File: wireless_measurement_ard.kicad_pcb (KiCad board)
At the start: 2 copper layers, 70 x 21.2 mm, 22 parts, among them J1 Conn_01x08, SW1 SW_SPDT, U2 JDY-08, U3 MCP16415, U4 MAX9938, U5 MAX9938, U6 EFM8LB1x-QFP32

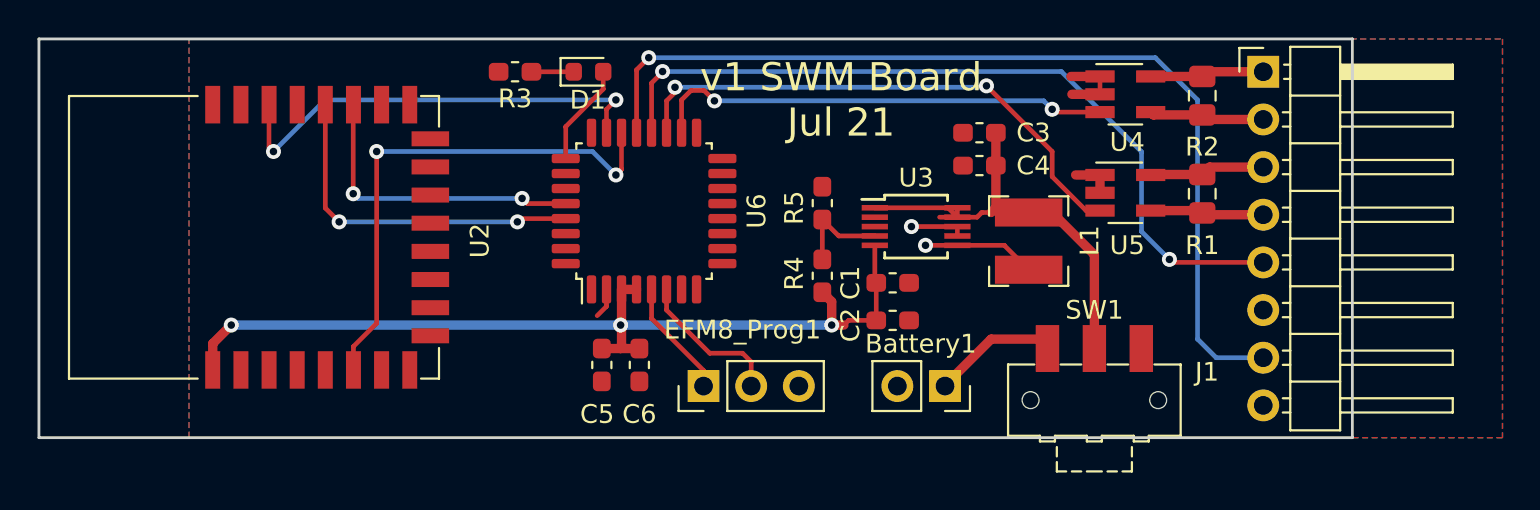
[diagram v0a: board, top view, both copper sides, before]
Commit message: update kicad to include holes
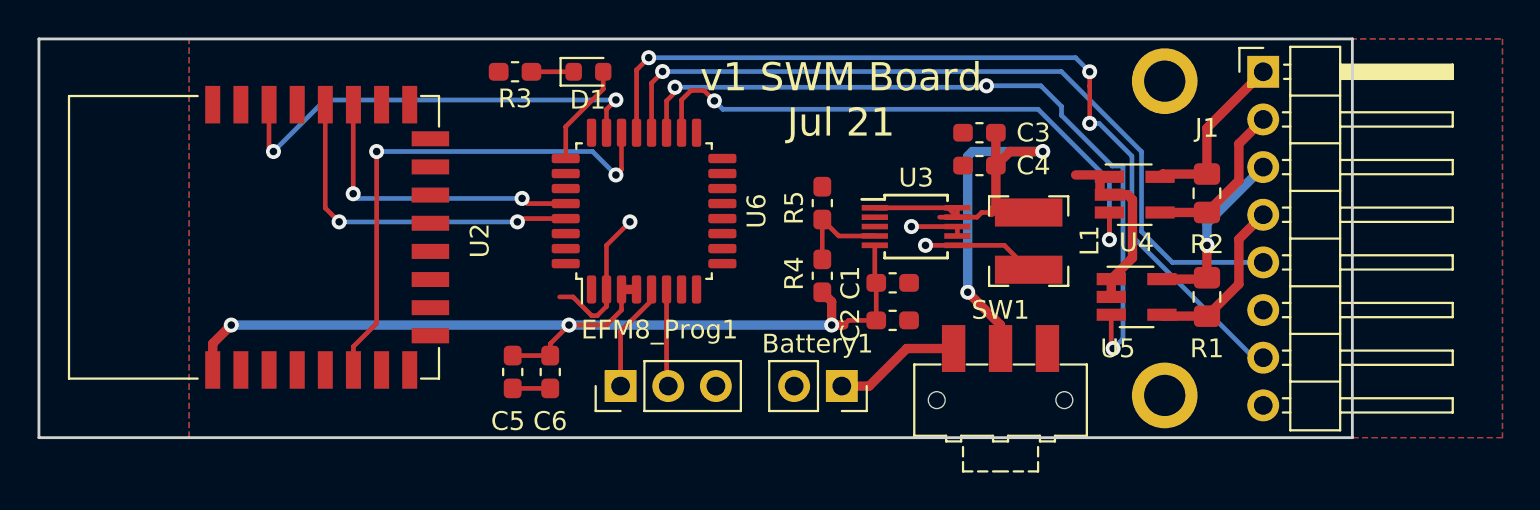
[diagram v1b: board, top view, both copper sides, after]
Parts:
- added H1: MountingHole_Pad, MountingHole:MountingHole_2.2mm_M2_ISO7380_Pad, F.Cu at (170.0, 94.0)
- added H2: MountingHole_Pad, MountingHole:MountingHole_2.2mm_M2_ISO7380_Pad, F.Cu at (170.0, 77.2)
- moved U5 5.58 mm to (168.5, 88.8)
- moved R1 5.51 mm to (172.2, 88.8)
- moved Battery1 5.50 mm to (152.8, 93.5)
- moved U4 5.37 mm to (168.4, 83.3)
- moved R2 5.21 mm to (172.2, 83.2)
- moved SW1 5.00 mm to (161.2, 94.2)
- moved C5 4.76 mm to (135.2, 92.8)
- moved C6 4.76 mm to (137.2, 92.8)
- moved EFM8_Prog1 4.42 mm to (141.0, 93.5)
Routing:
- net GND: track 10.8 -> 22.3 mm, vias 1 -> 2
- net A1: track 28.9 -> 40.4 mm, vias 2 -> 3
- net VIN: track 24.2 -> 33.5 mm, vias 0 -> 2
- net A0: track 24.7 -> 31.3 mm
- net C2_IN: track 6.17 -> 9.57 mm, vias 0 -> 1
- net A3: track 51.1 -> 47.7 mm, vias 1 -> 3
- net C1_IN: track 6.10 -> 9.25 mm
- net C2_OUT: track 6.09 -> 9.08 mm
- net +3V3: track 49.5 -> 52.3 mm
- net C2D: track 8.04 -> 5.19 mm
- net C1_OUT: track 6.16 -> 8.70 mm
- net Net-(SW1-Pad3): track 0.00 -> 0.85 mm
- net BATT: track 7.33 -> 6.79 mm
- net A2: vias 2 -> 1

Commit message: update to fix VIO
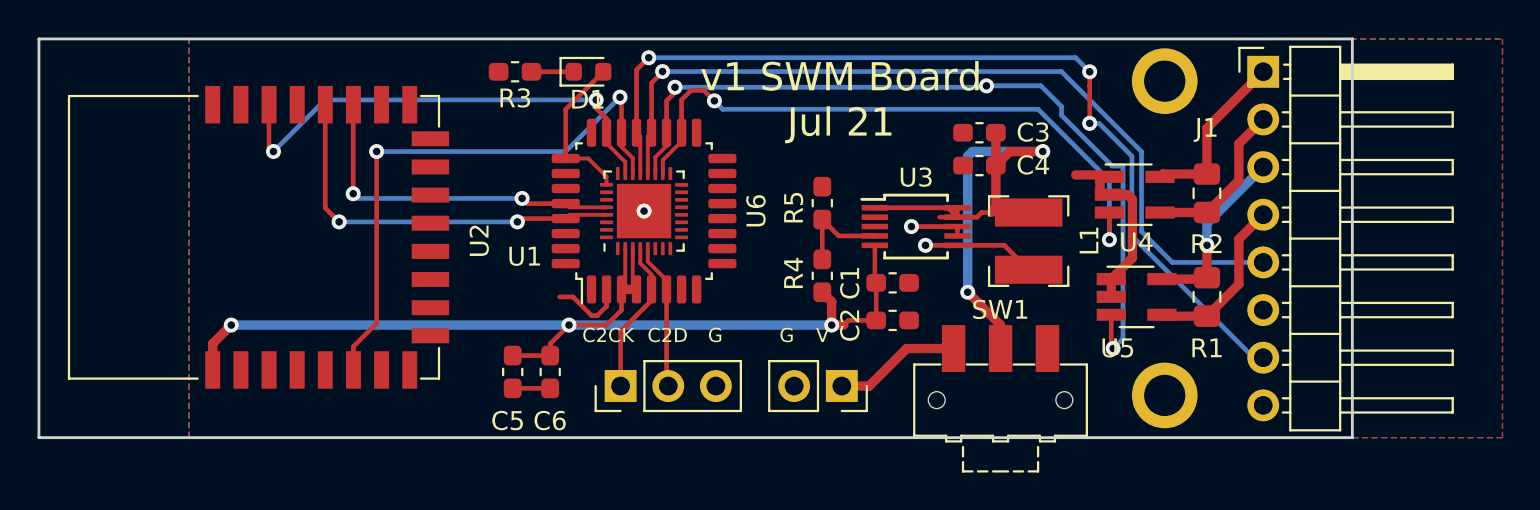
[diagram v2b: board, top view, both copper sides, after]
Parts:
- added U1: EFM8LB1, Package_DFN_QFN:QFN-32-1EP_4x4mm_P0.4mm_EP2.9x2.9mm, F.Cu at (142.2, 84.2)
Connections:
- net Net-(D1-Pad2) renamed LED
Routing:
- net +3V3: track 52.3 -> 56.9 mm
- net GND: track 22.3 -> 18.2 mm
- net LED: track 5.45 -> 8.46 mm
- net STATUS: track 27.8 -> 30.7 mm
- net C2D: track 5.19 -> 7.78 mm
- net A0: track 31.3 -> 33.9 mm
- net C2CK: track 5.83 -> 8.26 mm
- net A1: track 40.4 -> 42.9 mm
- net ARD_TX: track 18.7 -> 21.0 mm
- net A3: track 47.7 -> 50.0 mm
- net A2: track 42.2 -> 44.5 mm
- net ARD_RX: track 16.3 -> 18.6 mm
- net PWRC: track 23.9 -> 25.5 mm
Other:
- net class Default: clearance 0.2 -> 0.13
- rule trace_clearance: 0.2 -> 0.13
- board text added: "C2CK"
- board text added: "C2D"
- board text added: "G"
- board text added: "V"

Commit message: Halved the size of the board
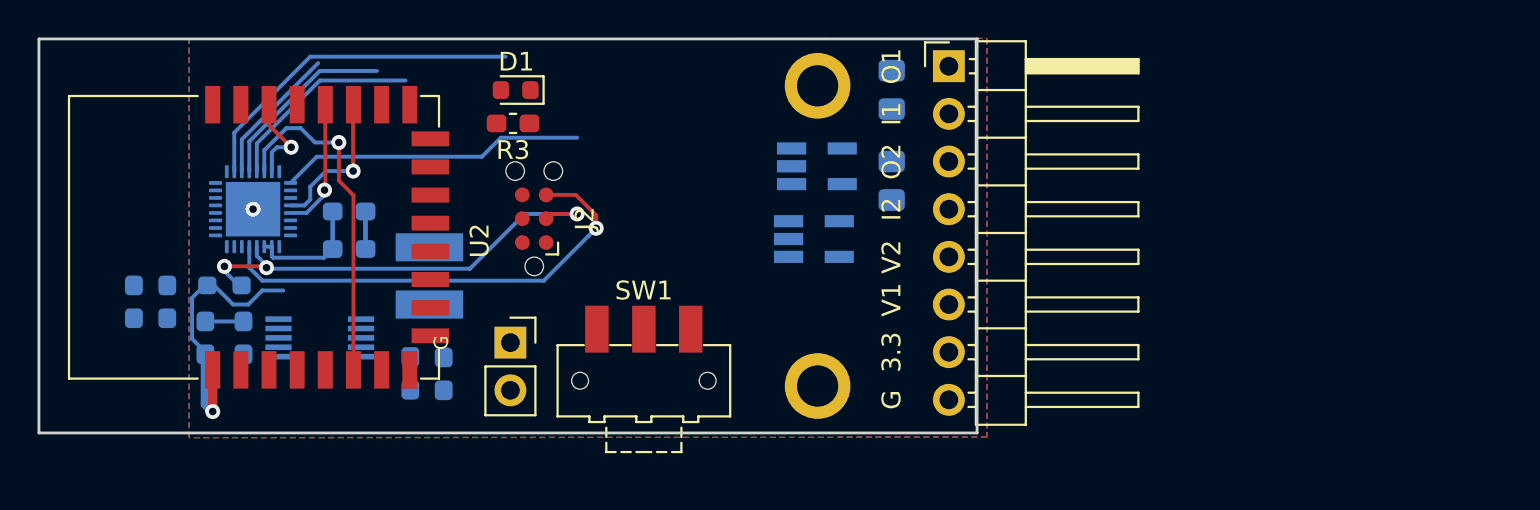
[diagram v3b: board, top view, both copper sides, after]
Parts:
- removed EFM8_Prog1: Conn_01x03, Connector_PinHeader_2.54mm:PinHeader_1x03_P2.54mm_Vertical
- removed the R1 at (172.2, 88.8)
- removed U6: EFM8LB1x-QFP32, Package_QFP:LQFP-32_7x7mm_P0.8mm
- added J2: Tag-Connect, Connector:Tag-Connect_TC2030-IDC-NL_2x03_P1.27mm_Vertical, F.Cu at (136.4, 84.6)
- added R2: 5R3, Resistor_SMD:R_0805_2012Metric_Pad1.15x1.40mm_HandSolder, B.Cu at (155.4, 82.6)
- added R6: 1k, Resistor_SMD:R_0603_1608Metric_Pad0.98x0.95mm_HandSolder, B.Cu at (119.9, 88.1)
- C1, C2, C3, C4, C5, C6, L1, R4, R5, U1, U3, U4, U5: moved to B.Cu
- R1: renamed from R2; moved to B.Cu
- moved C1 40.5 mm to (115.1, 89.0), turned to 270 degrees
- moved C2 38.7 mm to (116.8, 89.0), turned to 270 degrees
- moved R4 33.0 mm to (118.9, 90.9)
- moved U3 32.3 mm to (125.0, 90.9)
- moved C4 32.3 mm to (129.8, 92.8), turned to 270 degrees
- moved L1 32.0 mm to (130.8, 87.6)
- moved R5 31.7 mm to (120.9, 90.9), turned to 90 degrees
- moved C3 31.3 mm to (131.6, 92.9), turned to 270 degrees
- moved U1 20.8 mm to (121.4, 84.1)
- moved SW1 19.0 mm to (142.2, 93.2)
- moved H1 18.5 mm to (151.5, 93.5)
- moved H2 18.5 mm to (151.5, 77.5)
- moved Battery1 17.8 mm to (135.1, 91.2), turned to 0 degrees
- moved R1 17.7 mm to (155.4, 77.7), turned to 90 degrees
- moved U5 17.5 mm to (151.3, 85.7)
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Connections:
- J1 pad 1: C1_IN -> C1_OUT
- J1 pad 2: C1_OUT -> C1_IN
- J1 pad 3: C2_IN -> C2_OUT
- J1 pad 4: C2_OUT -> C2_IN
- J1 pad 6: GND -> A3
- J1 pad 7: A3 -> +3V3
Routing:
- net A3: track 50.0 -> 10.8 mm, vias 3 -> 0
- net +3V3: track 56.9 -> 21.2 mm, vias 3 -> 1
- net A1: track 42.9 -> 7.47 mm, vias 3 -> 0
- net A2: track 44.5 -> 9.97 mm, vias 1 -> 0
- net VIN: track 33.5 -> 0.00 mm, vias 2 -> 0
- net PWRC: track 25.5 -> 4.93 mm, vias 2 -> 1
- net C2D: track 7.78 -> 24.9 mm, vias 0 -> 1
- net C2CK: track 8.26 -> 24.6 mm, vias 0 -> 3
- net GND: track 18.2 -> 2.00 mm, vias 2 -> 1
- net A0: track 33.9 -> 18.2 mm, vias 2 -> 0
- net ARD_TX: track 21.0 -> 7.03 mm, vias 2 -> 1
- net STATUS: track 30.7 -> 18.4 mm, vias 2 -> 1
- net ARD_RX: track 18.6 -> 8.04 mm, vias 2 -> 1
- net C2_IN: track 9.57 -> 0.00 mm, vias 1 -> 0
- net C1_IN: track 9.25 -> 0.00 mm
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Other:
- board size 70 x 21.2 mm -> 50 x 21 mm
- board text added: "3.3"
- board text added: "I1"
- board text added: "I2"
- board text added: "O1"
- board text added: "O2"
- board text added: "SWM-mini Aug 21"
- board text added: "V1"
- board text added: "V2"
- board text removed: "C2CK"
- board text removed: "C2D"
- board text removed: "V"
- board text removed: "v1 SWM Board Jul 21"

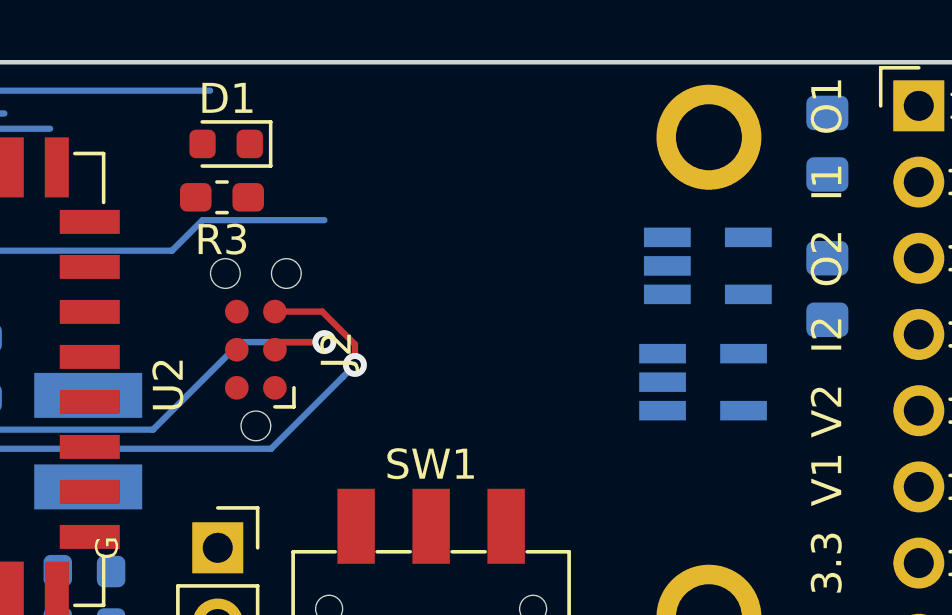
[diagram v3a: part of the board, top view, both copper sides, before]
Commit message: added high-voltage measurement
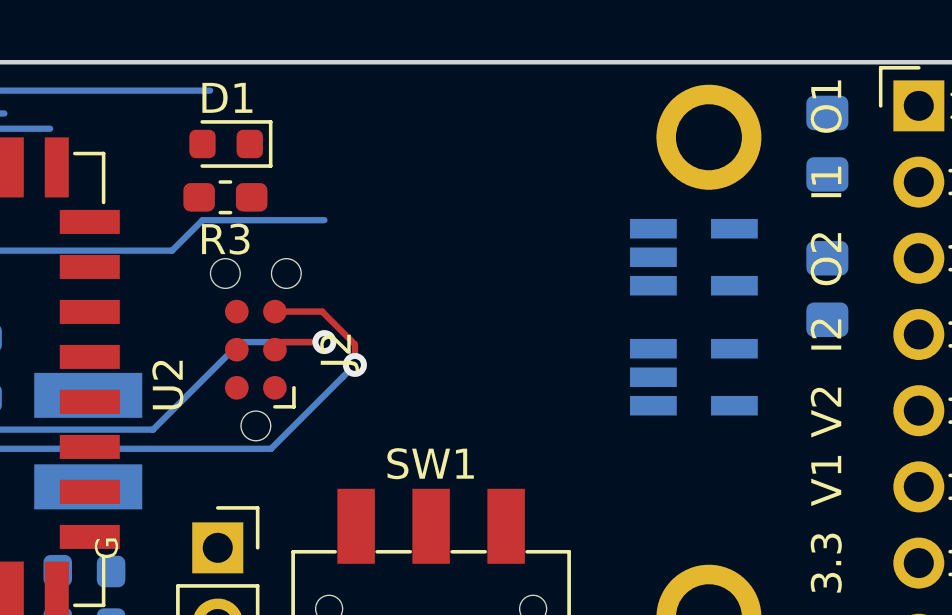
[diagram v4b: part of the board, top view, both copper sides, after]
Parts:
- moved U4 0.55 mm to (151.0, 81.5)
- moved U5 0.35 mm to (151.0, 85.5)
- moved R3 0.11 mm to (135.4, 79.5)
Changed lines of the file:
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@@
   )
   (module Package_TO_SOT_SMD:SOT-23-5_HandSoldering (layer B.Cu)
-    (at 151.464 81.788)
+    (at 151 81.5)
     (descr "5-pin SOT23 package")
     (tags "SOT-23-5 hand-soldering")
     (attr smd)
-    (fp_text reference U4 (at 0.1 -2.55) (layer B.SilkS)
+    (fp_text reference U4 (at -3.89 -0.254) (layer B.SilkS)
       (effects (font (size 1 1) (thickness 0.15)) (justify mirror))
     )
@@
   )
   (module Package_TO_SOT_SMD:SOT-23-5_HandSoldering (layer B.Cu)
-    (at 151.304 85.664)
+    (at 151 85.5)
     (descr "5-pin SOT23 package")
     (tags "SOT-23-5 hand-soldering")
     (attr smd)
-    (fp_text reference U5 (at -1 -2.75) (layer B.SilkS)
+    (fp_text reference U5 (at -3.934 0.098) (layer B.SilkS)
       (effects (font (size 1 1) (thickness 0.15)) (justify mirror))
     )
@@
     (tags "resistor handsolder")
     (attr smd)
-    (fp_text reference R1 (at 2.725 0 180) (layer B.SilkS)
+    (fp_text reference R1 (at -1.279 -1.524 270) (layer B.SilkS)
       (effects (font (size 1 1) (thickness 0.15)) (justify mirror))
     )
@@
     (tags "resistor handsolder")
     (attr smd)
-    (fp_text reference R2 (at 2.75 0 180) (layer B.SilkS)
+    (fp_text reference R2 (at -2.785 0 180) (layer B.SilkS)
       (effects (font (size 1 1) (thickness 0.15)) (justify mirror))
     )
@@
   )
   (module Resistor_SMD:R_0603_1608Metric_Pad1.05x0.95mm_HandSolder (layer F.Cu)
-    (at 135.269 79.502 180)
+    (at 135.382 79.502 180)
     (descr "Resistor SMD 0603 (1608 Metric), square (rectangular) end terminal, IPC_7351 nominal with elongated pad for handsoldering. (Body size source: http://www.tortai-tech.com/upload/download/2011102023233369053.pdf), generated with kicad-footprint-generator")
     (tags "resistor handsolder")
